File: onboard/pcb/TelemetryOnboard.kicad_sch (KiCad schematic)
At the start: 80 parts, among them J1 90 Deg. Socket 02x03 2.54mm, J2 Socket 01x02 2.54mm, J3 CONSMA001-SMD-G-T, J4 Socket 01x04 2.54mm, J5 Socket 01x02 2.54mm, U1 AVR128DB64x-xPT, U2 RC1780HP-RC232

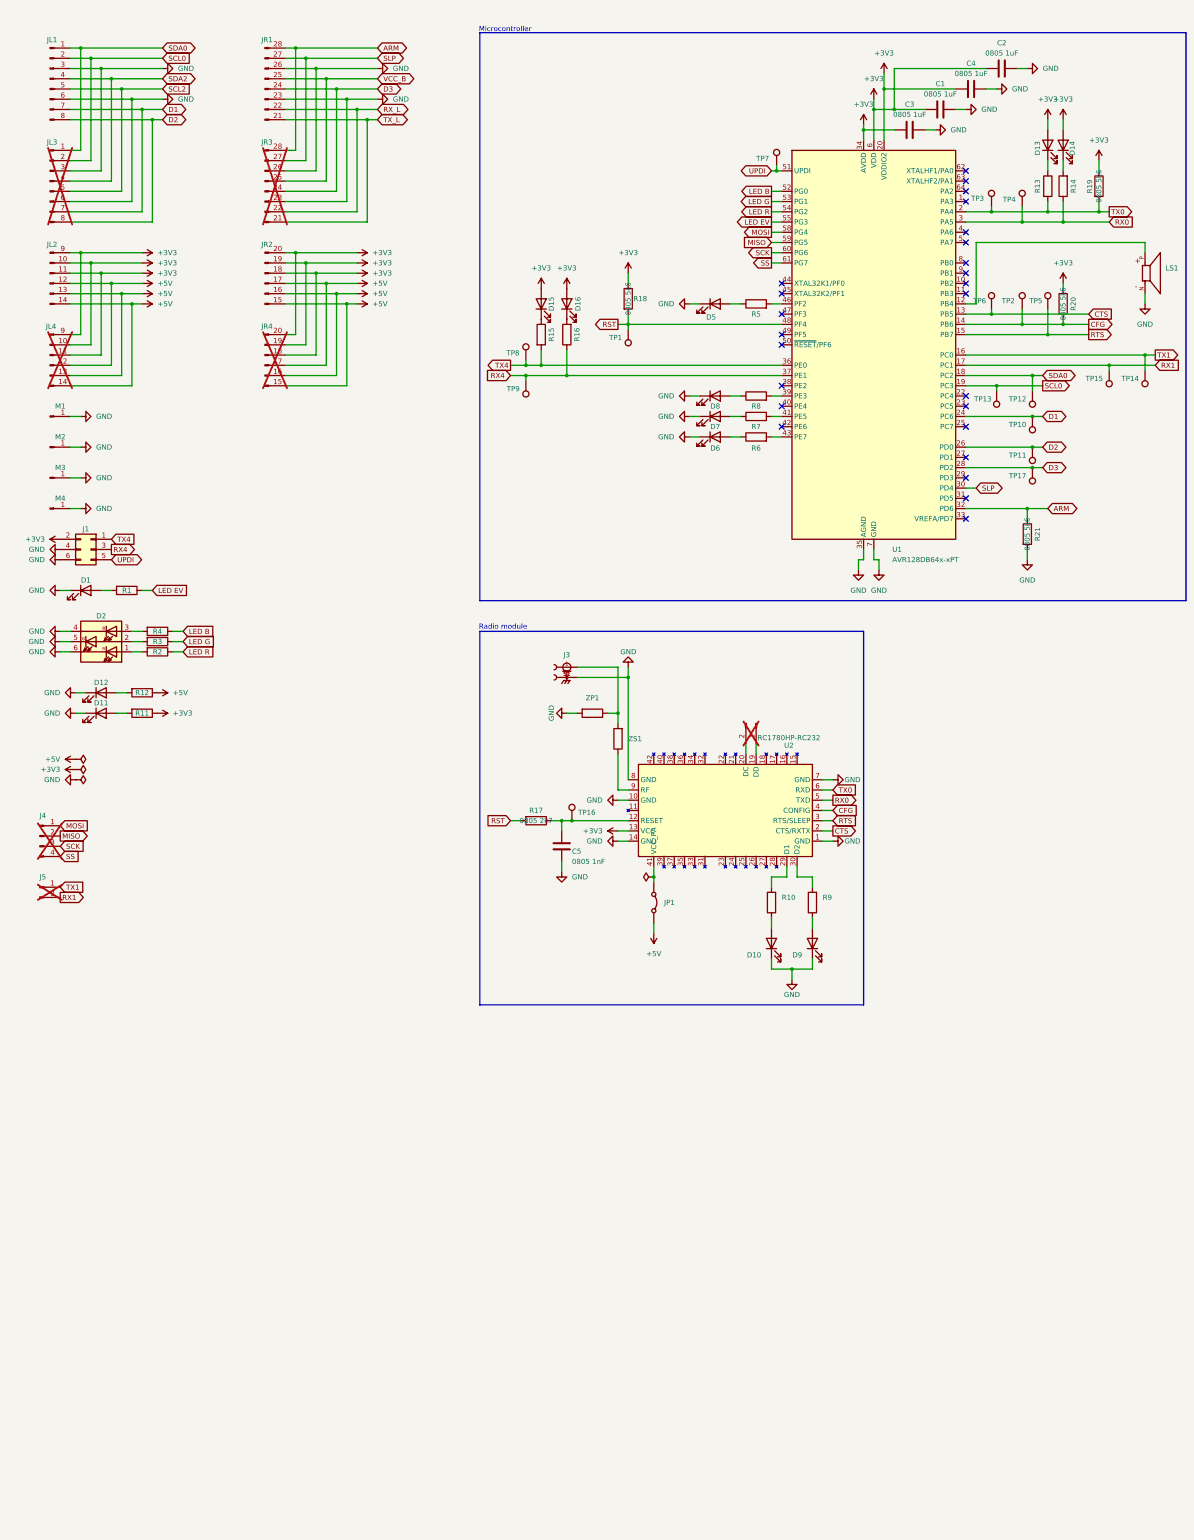
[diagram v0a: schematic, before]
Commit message: update pcb component 3d models, pcb bom, pcb schematic
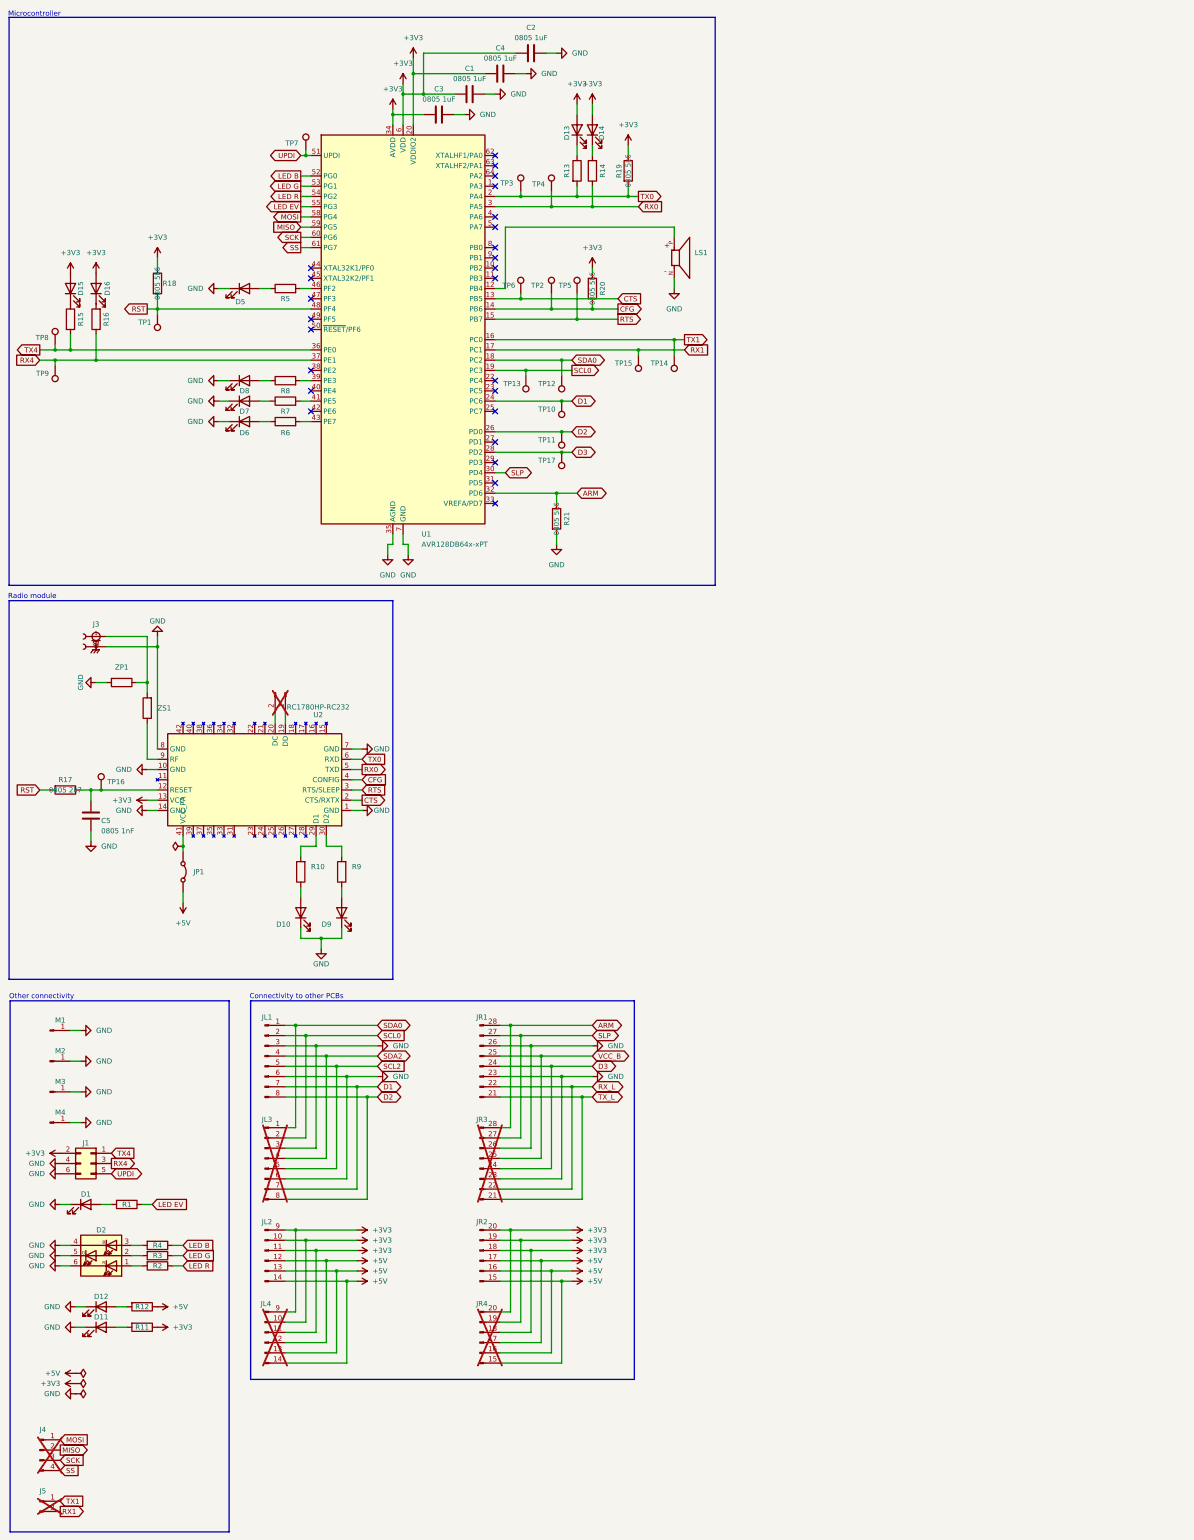
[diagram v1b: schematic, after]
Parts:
- J2, J4, J5: Purchase-URL (none) -> https://www.digikey.de/de/products/detail/sullins-connector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
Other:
- note added: "Connectivity to other PCBs"
- note added: "Other connectivity"
- moved on the sheet: C1, C2, C3, C4, C5, D1, D10, D11, D12, D13, D14, D15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

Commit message: first version new schematic
added symbols, footprints, 3dmodels, added new pcb base layout, added first schematic elements
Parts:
- removed D11: LED 0805 green, LED_SMD:LED_0805_2012Metric_Pad1.15x1.40mm_HandSolder, symbol Device:LED
- removed D2: CLS6B-FKW, Footprints:RGB LED Cree-PLCC-6_6x5mm_P2.1mm, symbol Library:RGB_LED_Cree-CLS6B-FKW
- removed D5, D8: LED 0805 orange, LED_SMD:LED_0805_2012Metric_Pad1.15x1.40mm_HandSolder, symbol Device:LED
- removed J1: 90 Deg. Socket 02x03 2.54mm, Connector_PinSocket_2.54mm:PinSocket_2x03_P2.54mm_Horizontal, symbol Connector_Generic:Conn_02x03_Odd_Even
- removed J2, J5: Socket 01x02 2.54mm, Connector_PinSocket_2.54mm:PinSocket_1x02_P2.54mm_Vertical, symbol Connector:Conn_01x02_Pin
- removed J4: Socket 01x04 2.54mm, Connector_PinSocket_2.54mm:PinSocket_1x04_P2.54mm_Vertical, symbol Connector:Conn_01x04_Pin
- removed JL1, JR1: Stackable Header 01x08 2.54mm, Connector_PinSocket_2.54mm:PinSocket_1x08_P2.54mm_Vertical, symbol Connector:Conn_01x08_Pin
- removed JL2, JR2: Stackable Header 01x06 2.54mm, Connector_PinSocket_2.54mm:PinSocket_1x06_P2.54mm_Vertical, symbol Connector:Conn_01x06_Pin
- removed JL3, JR3: ~, Connector_PinSocket_2.54mm:PinSocket_1x08_P2.54mm_Vertical, symbol Connector:Conn_01x08_Pin
- removed JL4, JR4: ~, Connector_PinSocket_2.54mm:PinSocket_1x06_P2.54mm_Vertical, symbol Connector:Conn_01x06_Pin
- removed JP1: ~, Footprints:Solder Jumper, symbol Jumper:Jumper_2_Bridged
- removed LS1: CMT-0525-75-SMT-TR, Footprints:Buzzer XDCR_CMT-0525-75-SMT-TR, symbol Library:Buzzer CMT-0525-75-SMT-TR
- removed R5, R6: 0805 270R, Resistor_SMD:R_0805_2012Metric_Pad1.20x1.40mm_HandSolder, symbol Device:R
- removed TP10, TP11, TP12, TP13, TP14, TP15, TP17: ~, Footprints:Test Point, symbol Connector:TestPoint
- removed U1: AVR128DB64x-xPT, Package_QFP:TQFP-64_10x10mm_P0.5mm, symbol MCU_Microchip_AVR_Dx:AVR128DB64x-xPT
- removed U2: RC1780HP-RC232, Footprints:Radiocrafts RC1780HP-RC232, symbol Library:Radiocrafts RC1780HP-RC232
- added C10, C11, C9 (x2): 0805 1uF, Capacitor_SMD:C_0805_2012Metric_Pad1.18x1.45mm_HandSolder, symbol Device:C
- added C12, C6, C8: 1 uf, symbol Device:C
- added C7: 0805 1nF, Capacitor_SMD:C_0805_2012Metric_Pad1.18x1.45mm_HandSolder, symbol Device:C
- added D11: BAT43, Diode_SMD:D_SOD-123, symbol Device:D_Schottky
- added D17: LED 0805 yellow, LED_SMD:LED_0805_2012Metric_Pad1.15x1.40mm_HandSolder, symbol Device:LED
- added D18: D, symbol Device:D
- added D19, D20, D21, D22, D23, D24: LED 0805 red, LED_SMD:LED_0805_2012Metric_Pad1.15x1.40mm_HandSolder, symbol Device:LED
- added D2, D3: orange, LED_SMD:LED_0805_2012Metric_Pad1.15x1.40mm_HandSolder, symbol Device:LED
- added D25, D26, D27, D28: LED 0805 orange, LED_SMD:LED_0805_2012Metric_Pad1.15x1.40mm_HandSolder, symbol Device:LED
- added D4: Cree RGB LED, Footprints:Cree RGB LED, symbol Symbols:Cree_RGB_LED
- added D5, D8: SP0503BAHT, Package_TO_SOT_SMD:SOT-143, symbol Power_Protection:SP0503BAHT
- added J1, J2: USB-C, Footprints:GCT_USB4215-03-A_REVA, symbol Symbols:USB4215-03-A_REVA
- added J4: CONSMA001-SMD-G-T, Footprints:SMA Connector CONSMA001-SMD-G-T, symbol Library:SMA Connector CONSMA001-SMD-G-T
- added JL1: Stackable Socket 1x8, Footprints:JL1, symbol Symbols:JL1_JL3
- added JL2: Stackable Socket 1x8, Footprints:JL2, symbol Symbols:JL2_JL4
- added JL3: Stackable Socket 1x8, Footprints:JL3, symbol Symbols:JL1_JL3
- added JL4: Stackable Socket 1x8, Footprints:JL4, symbol Symbols:JL2_JL4
- added JP1, JP2: SolderJumper_2_Open, Footprints:Solder Jumper, symbol Jumper:SolderJumper_2_Open
- added JR1: Stackable Socket 1x8, Footprints:JR1, symbol Symbols:JR1_JR3
- added JR2: Stackable Socket 1x8, Footprints:JR2, symbol Symbols:JR2_JR4
- added JR3: Stackable Socket 1x8, Footprints:JR3, symbol Symbols:JR1_JR3
- added JR4: Stackable Socket 1x8, Footprints:JR4, symbol Symbols:JR2_JR4
- added LS1: Buzzer CMT-0525-75-SMT-TR, Footprints:Buzzer XDCR_CMT-0525-75-SMT-TR, symbol Symbols:Buzzer CMT-0525-75-SMT-TR
- added Q1: NPN, symbol Simulation_SPICE:NPN
- added R2, R22, R3: 560 Ohm, Resistor_SMD:R_0805_2012Metric, symbol Device:R
- added R23, R26: 0805 2k7, Resistor_SMD:R_0805_2012Metric_Pad1.20x1.40mm_HandSolder, symbol Device:R
- added R24, R25, R27, R28, R45, R46, R47, R48: 0805 270R, Resistor_SMD:R_0805_2012Metric_Pad1.20x1.40mm_HandSolder, symbol Device:R
- added R29: 180 R, symbol Device:R
- added R30, R31: 10kR, symbol Device:R
- added R32, R33, R35, R36, R43, R44: 0805 1k, Resistor_SMD:R_0805_2012Metric_Pad1.20x1.40mm_HandSolder, symbol Device:R
- added R34, R37, R38, R39, R40, R41: 0805 5k6, Resistor_SMD:R_0805_2012Metric_Pad1.20x1.40mm_HandSolder, symbol Device:R
- added R42: 5.6k R, symbol Device:R
- added TP9: ~, Footprints:Test Point, symbol Connector:TestPoint
- added U1, U2: CP2102N, Footprints:QFN20_CP2102N_SIL, symbol Interface_USB:CP2102N-Axx-xQFN20
- added U3: RC1780HP-RC232, Footprints:Radiocrafts RC1780HP-RC232, symbol Library:Radiocrafts RC1780HP-RC232
- added U4: RC1701HP-RC232, Footprints:Radiocrafts RC1780HP-RC232, symbol Library:Radiocrafts RC1780HP-RC232
- added U5: AVR128DB64x-xPT, Package_QFP:TQFP-64_10x10mm_P0.5mm, symbol MCU_Microchip_AVR_Dx:AVR128DB64x-xPT
- added U6: W25Q80DVSSIG, Package_SO:SOIC-8_5.3x5.3mm_P1.27mm, symbol Memory_Flash:W25Q16JVSS
- added ZP2, ZS2: ~, Resistor_SMD:R_0805_2012Metric_Pad1.20x1.40mm_HandSolder, symbol Device:R
- C1, C3: value 0805 1uF -> 4.7 uF; Digikey Link https://www.digikey.de/de/products/detail/samsung-electro-m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 -> (none); Purchase-URL https://www.digikey.de/de/products/detail/samsung-electro-m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 -> (none)
- C2, C4: value 0805 1uF -> 0.1 uF; Digikey Link https://www.digikey.de/de/products/detail/samsung-electro-m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 -> (none); Purchase-URL https://www.digikey.de/de/products/detail/samsung-electro-m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 -> (none)
- D1, D7: value LED 0805 orange -> orange; Digikey Link https://www.digikey.de/de/products/detail/liteon/LTST-C170K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 -> (none); Purchase-URL https://www.digikey.de/de/products/detail/liteon/LTST-C170K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 -> (none)
- D10: value LED 0805 green -> orange; Digikey Link https://www.digikey.de/de/products/detail/liteon/LTST-C171G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 -> (none); Purchase-URL https://www.digikey.de/de/products/detail/liteon/LTST-C171G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 -> (none)
- D12: value LED 0805 green -> green; Digikey Link https://www.digikey.de/de/products/detail/liteon/LTST-C171G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 -> (none); Purchase-URL https://www.digikey.de/de/products/detail/liteon/LTST-C171G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 -> (none); now not fitted
- D13: value LED 0805 red -> green; Digikey Link https://www.digikey.de/de/products/detail/liteon/LTST-C171K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 -> (none); Purchase-URL https://www.digikey.de/de/products/detail/liteon/LTST-C171K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 -> (none); now not fitted
- D14, D16: value LED 0805 red -> LED 0805 green; Digikey Link https://www.digikey.de/de/products/detail/liteon/LTST-C171K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 -> https://www.digikey.de/de/products/detail/liteon/LTST-C171G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; Purchase-URL https://www.digikey.de/de/products/detail/liteon/LTST-C171K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 -> https://www.digikey.de/de/products/detail/liteon/LTST-C171G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
- D15: value LED 0805 red -> LED 0805 yellow; Digikey Link https://www.digikey.de/de/products/detail/liteon/LTST-C171K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 -> https://www.digikey.de/de/products/detail/liteon/LTST-C171Y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; Purchase-URL https://www.digikey.de/de/products/detail/liteon/LTST-C171K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 -> https://www.digikey.de/de/products/detail/liteon/LTST-C171Y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
- D6: value LED 0805 orange -> green; Digikey Link https://www.digikey.de/de/products/detail/liteon/LTST-C170K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 -> (none); Purchase-URL https://www.digikey.de/de/products/detail/liteon/LTST-C170K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 -> (none)
- D9: value LED 0805 yellow -> green; Digikey Link https://www.digikey.de/de/products/detail/liteon/LTST-C171Y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 -> (none); Purchase-URL https://www.digikey.de/de/products/detail/liteon/LTST-C171Y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 -> (none)
- M1, M2, M3, M4: value ~ -> M4 Mounting Hole; now in the parts list
- R1, R11, R12: value 0805 270R -> 560 Ohm; footprint Resistor_SMD:R_0805_2012Metric_Pad1.20x1.40mm_HandSolder -> Resistor_SMD:R_0805_2012Metric; Digikey Link https://www.digikey.de/de/products/detail/yageo/RC0805JR-07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 -> (none); Purchase-URL https://www.digikey.de/de/products/detail/yageo/RC0805JR-07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 -> (none)
- R10: value 0805 270R -> 22k; footprint Resistor_SMD:R_0805_2012Metric_Pad1.20x1.40mm_HandSolder -> Resistor_SMD:R_0805_2012Metric; Digikey Link https://www.digikey.de/de/products/detail/yageo/RC0805JR-07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 -> (none); Purchase-URL https://www.digikey.de/de/products/detail/yageo/RC0805JR-07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 -> (none)
- R13, R14: value 0805 1k -> 5k1; footprint Resistor_SMD:R_0805_2012Metric_Pad1.20x1.40mm_HandSolder -> Resistor_SMD:R_0805_2012Metric; Digikey Link https://www.digikey.de/de/products/detail/yageo/RC0805JR-13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 -> (none); Purchase-URL https://www.digikey.de/de/products/detail/yageo/RC0805JR-13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 -> (none)
- R15: value 0805 1k -> 47k; footprint Resistor_SMD:R_0805_2012Metric_Pad1.20x1.40mm_HandSolder -> Resistor_SMD:R_0805_2012Metric; Digikey Link https://www.digikey.de/de/products/detail/yageo/RC0805JR-13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 -> (none); Purchase-URL https://www.digikey.de/de/products/detail/yageo/RC0805JR-13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 -> (none)
- R16: value 0805 1k -> 22k; footprint Resistor_SMD:R_0805_2012Metric_Pad1.20x1.40mm_HandSolder -> Resistor_SMD:R_0805_2012Metric; Digikey Link https://www.digikey.de/de/products/detail/yageo/RC0805JR-13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 -> (none); Purchase-URL https://www.digikey.de/de/products/detail/yageo/RC0805JR-13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 -> (none)
- R17: value 0805 2k7 -> 560 Ohm; footprint Resistor_SMD:R_0805_2012Metric_Pad1.20x1.40mm_HandSolder -> Resistor_SMD:R_0805_2012Metric; Digikey Link https://www.digikey.de/de/products/detail/yageo/RC0805JR-07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 -> (none); Purchase-URL https://www.digikey.de/de/products/detail/yageo/RC0805JR-07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 -> (none)
- R18: value 0805 5k6 -> 560 Ohm; footprint Resistor_SMD:R_0805_2012Metric_Pad1.20x1.40mm_HandSolder -> Resistor_SMD:R_0805_2012Metric; Digikey Link https://www.digikey.de/de/products/detail/yageo/RC0805JR-07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 -> (none); Purchase-URL https://www.digikey.de/de/products/detail/yageo/RC0805JR-07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 -> (none)
- R19, R20: value 0805 5k6 -> 470 Ohm; footprint Resistor_SMD:R_0805_2012Metric_Pad1.20x1.40mm_HandSolder -> Resistor_SMD:R_0805_2012Metric; Digikey Link https://www.digikey.de/de/products/detail/yageo/RC0805JR-07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 -> (none); Purchase-URL https://www.digikey.de/de/products/detail/yageo/RC0805JR-07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 -> (none)
- R21: value 0805 5k6 -> 560 Ohm; footprint Resistor_SMD:R_0805_2012Metric_Pad1.20x1.40mm_HandSolder -> Resistor_SMD:R_0805_2012Metric; Digikey Link https://www.digikey.de/de/products/detail/yageo/RC0805JR-07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 -> (none); Purchase-URL https://www.digikey.de/de/products/detail/yageo/RC0805JR-07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 -> (none); now not fitted
- R4: renamed from R2; value 0805 270R -> 560 Ohm; footprint Resistor_SMD:R_0805_2012Metric_Pad1.20x1.40mm_HandSolder -> Resistor_SMD:R_0805_2012Metric; Digikey Link https://www.digikey.de/de/products/detail/yageo/RC0805JR-07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 -> (none); Purchase-URL https://www.digikey.de/de/products/detail/yageo/RC0805JR-07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 -> (none)
- R5: renamed from R3; value 0805 270R -> 560 Ohm; footprint Resistor_SMD:R_0805_2012Metric_Pad1.20x1.40mm_HandSolder -> Resistor_SMD:R_0805_2012Metric; Digikey Link https://www.digikey.de/de/products/detail/yageo/RC0805JR-07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 -> (none); Purchase-URL https://www.digikey.de/de/products/detail/yageo/RC0805JR-07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 -> (none)
- R6: renamed from R4; value 0805 270R -> 560 Ohm; footprint Resistor_SMD:R_0805_2012Metric_Pad1.20x1.40mm_HandSolder -> Resistor_SMD:R_0805_2012Metric; Digikey Link https://www.digikey.de/de/products/detail/yageo/RC0805JR-07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 -> (none); Purchase-URL https://www.digikey.de/de/products/detail/yageo/RC0805JR-07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 -> (none)
- R7, R8: value 0805 270R -> 5k1; footprint Resistor_SMD:R_0805_2012Metric_Pad1.20x1.40mm_HandSolder -> Resistor_SMD:R_0805_2012Metric; Digikey Link https://www.digikey.de/de/products/detail/yageo/RC0805JR-07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 -> (none); Purchase-URL https://www.digikey.de/de/products/detail/yageo/RC0805JR-07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 -> (none)
- R9: value 0805 270R -> 47k; footprint Resistor_SMD:R_0805_2012Metric_Pad1.20x1.40mm_HandSolder -> Resistor_SMD:R_0805_2012Metric; Digikey Link https://www.digikey.de/de/products/detail/yageo/RC0805JR-07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 -> (none); Purchase-URL https://www.digikey.de/de/products/detail/yageo/RC0805JR-07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 -> (none)
- TP1, TP2, TP3: value ~ -> TestPoint; now in the parts list
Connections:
- net ARM is gone; now on net +3V3: R21.1
- net CTS is gone; now on net RX0: TP6.1
- net RTS is gone; now on net TX0: TP5.1
- net +3V3: now also C2.1, C4.1, D10.2 (A), D6.2 (A), D7.2 (A), D9.2 (A), C10.1, C11.2, C12.2, C6.1, C8.1, C9.1, C9.2, D18.1 (K), D19.2 (A), D20.2 (A), D21.2 (A), D22.2 (A), D23.2 (A), D24.2 (A), JL2.10 (Pin_2), JL2.11 (Pin_3), JL2.9 (Pin_1), JL4.10 (Pin_2), JL4.11 (Pin_3), JL4.9 (Pin_1), JR2.22 (26), JR2.23 (Pin_2), JR2.24 (Pin_1), JR4.22 (26), JR4.23 (Pin_2), JR4.24 (Pin_1), LS1.P, R30.2, R31.1, R34.1, R37.1, R38.1, R39.1, R40.1, R41.1, R42.2, U1.6 (VDD), U1.7 (VREGIN), U2.6 (VDD), U2.7 (VREGIN), U3.13 (VCC), U4.13 (VCC), U4.41 (VCC_PA), U5.20 (VDDIO2), U5.34 (AVDD), U5.56 (VDD), U5.6 (VDD), U6.7 (~{HOLD}/~{RESET}/IO_{3}), U6.8 (VCC); no longer C2.2, C4.2, D13.2 (A), D14.2 (A), D15.2 (A), D16.2 (A), R11.1, R18.1, R19.1, R20.1
- net +5V: now also JL2.12 (Pin_4), JL2.13 (Pin_5), JL2.14 (Pin_6), JL4.12 (Pin_4), JL4.13 (Pin_5), JL4.14 (Pin_6), JR2.19 (Pin_6), JR2.20 (Pin_5), JR2.21 (Pin_4), JR4.19 (Pin_6), JR4.20 (Pin_5), JR4.21 (Pin_4), R22.1, U3.41 (VCC_PA); no longer R12.1
- net GND: now also C2.2, C4.2, D13.1 (K), D14.1 (K), D15.1 (K), D16.1 (K), R13.2, R14.2, R15.2, R7.2, R8.2, R9.2, C10.2, C11.1, C12.1, C6.2, C7.2, C8.2, C9.1, C9.2, D17.1 (K), D2.1 (K), D25.1 (K), D26.1 (K), D27.1 (K), D28.1 (K), D3.1 (K), D4.4 (KB), D4.5 (KR), D4.6 (KR), D5.1 (A), D8.1 (A), J1.A1_B12 (GND_A), J1.B1_A12 (GND_B), J1.SH1 (SHIELD), J1.SH2 (SHIELD), J1.SH3 (SHIELD), J1.SH4 (SHIELD), J2.A1_B12 (GND_A), J2.B1_A12 (GND_B), J2.SH1 (SHIELD), J2.SH2 (SHIELD), J2.SH3 (SHIELD), J2.SH4 (SHIELD), J4.S1, J4.S2, JL1.3 (Pin_3), JL1.6 (Pin_6), JL3.3 (Pin_3), JL3.6 (Pin_6), JP1.2 (B), JP2.2 (B), JR1.25 (Pin_8), JR1.29 (Pin_4), JR3.25 (Pin_8), JR3.29 (Pin_4), Q1.3 (E), U1.12 (GND), U1.21 (GND), U1.3 (GND), U2.12 (GND), U2.21 (GND), U2.3 (GND), U3.1 (GND), U3.10 (GND), U3.14 (GND), U3.7 (GND), U3.8 (GND), U4.1 (GND), U4.10 (GND), U4.14 (GND), U4.7 (GND), U4.8 (GND), U5.21 (GND), U5.35 (AGND), U5.57 (GND), U5.7 (GND), U6.4 (GND), ZP2.2; no longer C2.1, C4.1, D10.1 (K), D6.1 (K), D7.1 (K), D9.1 (K), R21.2
- net LED B: now also U5.42 (PE6)
- net LED G: now also U5.43 (PE7)
- net LED R: now also U5.44 (XTAL32K1/PF0)
- net RX0: now also R33.1, U3.5 (TXD), U5.3 (PA5); no longer R14.1, TP4.1
- net RX1: now also TP8.1, R36.1, U4.5 (TXD), U5.17 (PC1)
- net RX4: now also TP1.1, R44.1, U1.18 (TXD), U5.41 (PE5); no longer R16.1
- net SLP: now also JR1.30 (26), JR3.30 (26), U5.52 (PG0)
- net TX0: now also R32.2, R34.2, U3.6 (RXD), U5.2 (PA4); no longer R13.2, R19.2, TP3.1
- net TX1: now also TP7.1, R35.2, R37.2, U4.6 (RXD), U5.16 (PC0)
- net TX4: now also TP2.1, R43.2, TP9.1, U1.17 (RXD), U5.40 (PE4); no longer R15.2, TP8.1
- net UPDI: now also R20.1, TP3.1, U5.51 (UPDI); no longer TP7.1
- net at R16.2: now also R15.1, U2.8 (VBUS); no longer D16.1 (K)
- net at R4.2: now also D4.1 (AR)
- net at R5.2: now also D4.2 (AG)
- net at R6.2: now also D4.3 (AB)
- net VBUS1: now reaches R10.1
- net VBUS1: now also D5.2 (K), J1.A4_B9 (VBUS_A), J1.B4_A9 (VBUS_B); no longer D10.2 (A)
- net at R11.2: now also U1.20 (~{TXT}/GPIO.2)
- net at R8.1: now also J1.B5 (CC2)
- net at R7.1: now also J1.A5 (CC1); no longer D7.2 (A)
- net at R13.1: now also J2.A5 (CC1); no longer D13.1 (K)
- net at C5.1, TP16.1: now also R23.1, U3.12 (RESET); no longer R17.1
- net at D12.2 (A): now also R21.2; no longer R12.2
- net at ZS1.1: now also U3.9 (RF)
- net at R9.1: now also R10.2, U1.8 (VBUS); no longer D9.2 (A)
- net CFG: no longer names the net of R20.2
- net CFG: now also D11.2 (A), U2.17 (RXD); no longer TP2.1
- net LED EV renamed LED 1
- net LED 1: now also U5.45 (XTAL32K2/PF1)
- removed net RST: R17.2, R18.2, TP1.1
- new net: D3.2 (A), R3.2
- new net: C7.1, R26.1, TP4.1, U4.12 (RESET)
- new net: J2.B5 (CC2), R14.1
- new net: D14.2 (A), R24.1
- new net: R24.2, U3.29 (D1)
- new net: R25.2, U3.30 (D2)
- new net: D22.1 (K), R36.2
- new net: JP2.1 (A), U2.15 (~{CTS})
- new net: D19.1 (K), R32.1
- new net: D10.1 (K), R18.1
- new net: D2.2 (A), R2.2
- new net: D7.1 (K), R12.1
- new net: R12.2, U1.19 (~{RXT}/GPIO.3)
- new net: R27.2, U4.29 (D1)
- new net: R28.2, U4.30 (D2)
- new net: U4.9 (RF), ZS2.1
- new net: JP1.1 (A), U1.15 (~{CTS})
- new net: D25.2 (A), R45.1
- new net: D11.1 (K), R19.1
- new net: D24.1 (K), R44.2
- new net: D17.2 (A), R28.1
- new net: D9.1 (K), R17.1
- new net: R17.2, U2.20 (~{TXT}/GPIO.2)
- new net: D18.2 (A), LS1.N, Q1.1 (C)
- new net: D28.2 (A), R48.1
- new net: J4.1, ZP2.1, ZS2.2
- new net: D15.2 (A), R25.1
- new net: R47.2, U5.26 (PD0)
- new net: R46.2, U5.28 (PD2)
- new net: R45.2, U5.30 (PD4)
- new net: R48.2, U5.32 (PD6)
- new net: R29.2, U5.9 (PB1)
- new net: R19.2, U2.18 (TXD)
- new net: D26.2 (A), R46.1
- new net: D6.1 (K), R11.1
- new net: R18.2, U2.19 (~{RXT}/GPIO.3)
- new net: D27.2 (A), R47.1
- new net: Q1.2 (B), R29.1
- new net: D13.2 (A), R22.2
- new net: D23.1 (K), R43.1
- new net: D16.2 (A), R27.1
- new net: D21.1 (K), R35.1
- new net: D20.1 (K), R33.2
- new net +3V_LP: JL2.16 (Pin_8), JL4.16 (Pin_8), JR2.17 (Pin_8), JR4.17 (Pin_8)
- new net +V_BATT: JL2.15 (Pin_7), JL4.15 (Pin_7), JR2.18 (Pin_7), JR4.18 (Pin_7)
- new net ARM1: JR1.31 (Pin_2), JR3.31 (Pin_2), U5.53 (PG1)
- new net ARM2: JR1.32 (Pin_1), JR3.32 (Pin_1)
- new net CFG1: R41.2, U3.4 (CONFIG), U5.5 (PA7)
- new net CFG2: R40.2, U4.4 (CONFIG), U5.15 (PB7)
- new net CS0: R42.1, U5.39 (PE3), U6.1 (~{CS})
- new net CTS1: U3.2 (CTS/RXTX), U5.4 (PA6)
- new net CTS2: U4.2 (CTS/RXTX), U5.14 (PB6)
- new net D+1: D5.4 (K), J1.A6 (DP1), J1.B6 (DP2), U1.4 (D+)
- new net D+2: D8.4 (K), J2.A6 (DP1), J2.B6 (DP2), U2.4 (D+)
- new net D-1: D5.3 (K), J1.A7 (DN1), J1.B7 (DN2), U1.5 (D-)
- new net D-2: D8.3 (K), J2.A7 (DN1), J2.B7 (DN2), U2.5 (D-)
- new net D26: JR1.26 (Pin_7), JR3.26 (Pin_7), U5.48 (PF4)
- new net D27: JR1.27 (Pin_6), JR3.27 (Pin_6), U5.49 (PF5)
- new net D28: JR1.28 (Pin_5), JR3.28 (Pin_5), U5.50 (~{RESET}/PF6)
- new net D4: JL1.4 (Pin_4), JL3.4 (Pin_4), U5.22 (PC4)
- new net D5: JL1.5 (Pin_5), JL3.5 (Pin_5), U5.23 (PC5)
- new net LED 2: R2.1, U5.46 (PF2)
- new net LED 3: R3.1, U5.47 (PF3)
- new net MISO0: U5.37 (PE1), U6.2 (DO/IO_{1})
- new net MOSI0: U5.36 (PE0), U6.5 (DI/IO_{0})
- new net RST1: R23.2, R38.2, U5.1 (PA3)
- new net RST2: R26.2, R39.2, U5.12 (PB4)
- new net RTS1: U3.3 (RTS/SLEEP), U5.8 (PB0)
- new net RTS2: U4.3 (RTS/SLEEP), U5.13 (PB5)
- new net RX_BUS: JL1.7 (Pin_7), JL3.7 (Pin_7)
- new net SCK0: U5.38 (PE2), U6.6 (CLK)
- new net SCL1: JL1.2 (Pin_2), JL3.2 (Pin_2), R30.1, U5.19 (PC3)
- new net SDA1: JL1.1 (Pin_1), JL3.1 (Pin_1), R31.2, U5.18 (PC2)
- new net TX_BUS: JL1.8 (Pin_8), JL3.8 (Pin_8)
- new net VBUS2: D8.2 (K), J2.A4_B9 (VBUS_A), J2.B4_A9 (VBUS_B), R16.1
- no-connect marks 25 -> 33
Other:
- note added: "Flash Storage"
- note added: "Mounting Holes"
- note added: "Pinheader / PCB Bus"
- note added: "Pinheader?"
- note added: "Power LEDs"
- note added: "Radio module (169 MHz)"
- note added: "Radio module (869.5 MHz)"
- note added: "Status LEDs"
- note added: "USB UART"
- note added: "USB UPDI"
- note removed: "Connectivity to other PCBs"
- note removed: "Other connectivity"
- note removed: "Radio module"
- company: Spaceflight Rocketry Giessen e.V. -> (none)
- title: Onboard Telemetry -> (none)
- moved on the sheet: C5, D1, J3, M1, M2, M3, M4, R1, R4, R5, R6, TP16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

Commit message: update onboard schematic
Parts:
- added TP1, TP12, TP13, TP14, TP15, TP18, TP19, TP22, TP23, TP36, TP37, TP38, TP39, TP4, TP48, TP49, TP5, TP50, TP51, TP52, TP53, TP8, TP9: TestPoint, symbol Connector:TestPoint
- R42: value 5.6k R -> 5.6kR
- renumbered TP7 to TP16, TP8 to TP17, TP5 to TP2, TP6 to TP3, TP9 to TP40, TP9 to TP41
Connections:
- net ARM1: now also TP53.1
- net CFG1: now also TP5.1
- net CFG2: now also TP15.1
- net CS0: now also TP39.1
- net CTS1: now also TP4.1
- net CTS2: now also TP14.1
- net D26: now also TP48.1
- net D27: now also TP49.1
- net D28: now also TP50.1
- net D4: now also TP22.1
- net D5: now also TP23.1
- net MISO0: now also TP37.1
- net MOSI0: now also TP36.1
- net RST1: now also TP1.1
- net RST2: now also TP12.1
- net RTS1: now also TP8.1
- net RTS2: now also TP13.1
- net SCK0: now also TP38.1
- net SCL1: now also TP19.1
- net SDA1: now also TP18.1
- net SLP: now also TP52.1
- net UPDI: now also TP51.1
- net at R29.2, U5.9 (PB1): now also TP9.1
- no-connect marks 33 -> 40
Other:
- note added: "Flags"
- moved on the sheet: C1, C10, C11, C12, C2, C3, C4, C5, C6, C7, C8, C9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

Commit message: update platine
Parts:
- removed TP18, TP19, TP22, TP23, TP48, TP49, TP50, TP51, TP52, TP53: TestPoint, symbol Connector:TestPoint
- removed TP40, TP41: ~, Footprints:Test Point, symbol Connector:TestPoint
- C15: renamed from C12; footprint (none) -> Capacitor_SMD:C_0805_2012Metric_Pad1.18x1.45mm_HandSolder
- C6, C8: footprint (none) -> Capacitor_SMD:C_0805_2012Metric_Pad1.18x1.45mm_HandSolder
- D18: footprint (none) -> Diode_SMD:D_SOD-123
- J3, J4: symbol Library:SMA Connector CONSMA001-SMD-G-T -> Symbols:SMA Connector CONSMA001-SMD-G-T; Purchase-URL https://www.digikey.de/de/products/detail/te-connectivity-l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 -> https://www.snapeda.com/api/url_track_click_mouser/?unipart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
- Q1: footprint (none) -> Package_TO_SOT_SMD:SOT-23
- R1, R10, R11, R12, R13, R14, R15, R16, R17, R18, R19, R2, R20, R21, R22, R3, R4, R5, R6, R7, R8, R9: footprint Resistor_SMD:R_0805_2012Metric -> Resistor_SMD:R_0805_2012Metric_Pad1.20x1.40mm_HandSolder
- R29, R30, R31, R42: footprint (none) -> Resistor_SMD:R_0805_2012Metric_Pad1.20x1.40mm_HandSolder
- TP1, TP12, TP13, TP14, TP15, TP36, TP37, TP38, TP39, TP4, TP5, TP8, TP9: footprint (none) -> Footprints:Test Point
- U3, U4: symbol Library:Radiocrafts RC1780HP-RC232 -> Symbols:Radiocrafts RC1780HP-RC232
- renumbered C9 to C12, TP2 to TP18, TP1 to TP19, TP16 to TP40, TP3 to TP41, TP4 to TP42

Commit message: update platine radio module led
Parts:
- renumbered TP19 to TP1, TP18 to TP2, TP41 to TP3, TP1 to TP60, TP2 to TP70, TP3 to TP80
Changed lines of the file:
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@@
 		(on_board yes)
 		(dnp no)
-		(property "Reference" "TP41"
+		(property "Reference" "TP3"
 			(at 271.272 223.52 0)
 			(effects
@@
 			(project "Platinenkonzept v3.0.0"
 				(path "/a51e9d97-2dc7-47e6-bab2-df98d7ad5ab9"
-					(reference "TP41")
+					(reference "TP3")
 					(unit 1)
 				)
@@
 		(on_board yes)
 		(dnp no)
-		(property "Reference" "TP18"
+		(property "Reference" "TP2"
 			(at 103.632 214.63 0)
 			(effects
@@
 			(project "Platinenkonzept v3.0.0"
 				(path "/a51e9d97-2dc7-47e6-bab2-df98d7ad5ab9"
-					(reference "TP18")
+					(reference "TP2")
 					(unit 1)
 				)
@@
 		(on_board yes)
 		(dnp no)
-		(property "Reference" "TP3"
+		(property "Reference" "TP80"
 			(at 465.074 234.442 0)
 			(effects
@@
 			(project "TelemetryOnboard"
 				(path "/a51e9d97-2dc7-47e6-bab2-df98d7ad5ab9"
-					(reference "TP3")
+					(reference "TP80")
 					(unit 1)
 				)
@@
 		(on_board yes)
 		(dnp no)
-		(property "Reference" "TP2"
+		(property "Reference" "TP70"
 			(at 459.74 234.188 0)
 			(effects
@@
 			(project "TelemetryOnboard"
 				(path "/a51e9d97-2dc7-47e6-bab2-df98d7ad5ab9"
-					(reference "TP2")
+					(reference "TP70")
 					(unit 1)
 				)
@@
 		(on_board yes)
 		(dnp no)
-		(property "Reference" "TP19"
+		(property "Reference" "TP1"
 			(at 106.172 219.71 0)
 			(effects
@@
 			(project ""
 				(path "/a51e9d97-2dc7-47e6-bab2-df98d7ad5ab9"
-					(reference "TP19")
+					(reference "TP1")
 					(unit 1)
 				)
@@
 		(dnp no)
 		(fields_autoplaced yes)
-		(property "Reference" "TP1"
+		(property "Reference" "TP60"
 			(at 452.12 231.6479 0)
 			(effects
@@
 			(project "TelemetryOnboard"
 				(path "/a51e9d97-2dc7-47e6-bab2-df98d7ad5ab9"
-					(reference "TP1")
+					(reference "TP60")
 					(unit 1)
 				)

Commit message: Led resistor from 270 to 560+
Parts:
- R24, R25, R27, R28: value 0805 270R -> 0805 560R
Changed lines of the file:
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@@
 			)
 		)
-		(property "Value" "0805 270R"
+		(property "Value" "0805 560R"
 			(at 337.82 100.3299 0)
 			(effects
@@
 			)
 		)
-		(property "Value" "0805 270R"
+		(property "Value" "0805 560R"
 			(at 232.41 100.3299 0)
 			(effects
@@
 			)
 		)
-		(property "Value" "0805 270R"
+		(property "Value" "0805 560R"
 			(at 222.25 100.3299 0)
 			(effects
@@
 			)
 		)
-		(property "Value" "0805 270R"
+		(property "Value" "0805 560R"
 			(at 347.98 100.3299 0)
 			(effects

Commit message: clean up schematic and add tht sma conn
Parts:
- removed J3, J4: CONSMA001-SMD-G-T, Footprints:SMA Connector CONSMA001-SMD-G-T, symbol Symbols:SMA Connector CONSMA001-SMD-G-T
- removed TP40, TP42: ~, Footprints:Test Point, symbol Connector:TestPoint
- added J3, J4: RFPC-SMA28-F, Footprints:RFPC-SMA28-F, symbol Symbols:RFPC-SMA28-F
- added R49, R50: 5k6, Resistor_SMD:R_0805_2012Metric_Pad1.20x1.40mm_HandSolder, symbol Device:R
- C10, C11, C12, C9: value 0805 1uF -> 1 uF
- C5, C7: value 0805 1nF -> 1 nF
- D14, D16: value LED 0805 green -> green
- D15, D17: value LED 0805 yellow -> yellow
- D19, D20, D21, D22, D23, D24: value LED 0805 red -> red
- D25, D26, D27, D28: value LED 0805 orange -> orange
- R23, R26: value 0805 2k7 -> 2k7
- R24, R25, R27, R28: value 0805 560R -> 560R
- R30, R31: value 10kR -> 5k6
- R32, R33, R35, R36, R43, R44: value 0805 1k -> 1k
- R34, R37, R38, R39, R40, R41: value 0805 5k6 -> 5k6; Digikey Link https://www.digikey.de/de/products/detail/yageo/RC0805JR-07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 -> (none); Purchase-URL https://www.digikey.de/de/products/detail/yageo/RC0805JR-07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 -> (none)
- R42: value 5.6kR -> 5k6
- R45, R46, R47, R48: value 0805 270R -> 270R
- TP16, TP17, TP70, TP80: value ~ -> TestPoint; now in the parts list
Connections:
- net +3V3: now also R31.2, R34.2, R37.2, R38.2, R39.2, R40.2, R41.2; no longer R31.1, R34.1, R37.1, R38.1, R39.1, R40.1, R41.1
- net ARM1: now also R49.1
- net CFG1: now also R41.1; no longer R41.2
- net CFG2: now also R40.1; no longer R40.2
- net GND: now also J3.G1, J3.G2, J3.G3, J3.G4, J4.G1, J4.G2, J4.G3, J4.G4, R49.2, R50.2
- net RST1: now also R38.1; no longer R38.2
- net RST2: now also R39.1; no longer R39.2
- net SDA1: now also R31.1; no longer R31.2
- net SLP: now also R50.1
- net TX0: now also R34.1; no longer R34.2
- net TX1: now also R37.1; no longer R37.2
- net BUZZ: now reaches R29.2, TP9.1, U5.9 (PB1)
- net at ZP2.1, ZS2.2: now also J4.1
- net at ZP1.1, ZS1.2: now also J3.1
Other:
- note added: "Buzzer"
- note added: "Pull-Up / Pull-Down"
- note added: "Test Points"
- moved on the sheet: C1, C10, C11, C12, C2, C3, C4, C9, D10, D11, D18, D19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
